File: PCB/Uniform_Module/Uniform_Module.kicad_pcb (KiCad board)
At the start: 2 copper layers, 301.5 x 93.4 mm, 186 parts, among them M1 MountingHole_2.7mm_M2.5, M10 MountingHole_2.7mm_M2.5, M2 MountingHole_2.7mm_M2.5, M3 MountingHole_2.7mm_M2.5, M4 MountingHole_2.7mm_M2.5, M5 MountingHole_2.7mm_M2.5, M6 MountingHole_2.7mm_M2.5, M7 MountingHole_2.7mm_M2.5, M8 MountingHole_2.7mm_M2.5, M9 MountingHole_2.7mm_M2.5, U1 STM32L072KZT6, U2 SN74AHCT1G125DBVR

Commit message: PCIE slot is upside down... began footprint, comitting changes and preparing to re-route on board :(
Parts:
- removed C1, C2: 10uf, ul_FG16X7R1E106KRT06:FG16X7R1E106KRT06
- removed C3, C4, C5: 0.1uf, Resistor_THT:R_Axial_DIN0207_L6.3mm_D2.5mm_P7.62mm_Horizontal
- removed C6: 1uf, RDER71H105K2M1H03A:CAP_RDER71H105K2M1H03A
- removed D_0_0, D_0_1, D_0_10, D_0_11, D_0_12, D_0_13, D_0_2, D_0_3, D_0_4, D_0_5, D_0_6, D_0_7, D_0_8, D_0_9, D_1_0, D_1_1, D_1_10, D_1_11, D_1_12, D_1_13, D_1_2, D_1_3, D_1_4, D_1_5, D_1_6, D_1_7, D_1_8, D_1_9, D_2_0, D_2_1, D_2_10, D_2_11, D_2_12, D_2_13, D_2_2, D_2_3, D_2_4, D_2_5, D_2_6, D_2_7, D_2_8, D_2_9, D_3_0, D_3_1, D_3_10, D_3_11, D_3_12, D_3_13, D_3_2, D_3_3, D_3_4, D_3_5, D_3_6, D_3_7, D_3_8, D_3_9, D_4_0, D_4_1, D_4_10, D_4_11, D_4_12, D_4_13, D_4_2, D_4_4, D_4_5, D_4_6, D_4_8, D_4_9: D, 1N4148:DIOAD829W49L456D191
- removed EM1, EM2, M1, M10, M2, M3, M4, M5, M6, M7, M8, M9: MountingHole_2.7mm_M2.5, MountingHole:MountingHole_2.7mm_M2.5
- removed G*** (x12): LOGO, Graphics:graphic_mounting_indicator
- removed G*** (x2): LOGO, Graphics:graphic_logo
- removed G***: LOGO, Graphics:graphic_designed-by-with-year
- removed K_0_0, K_0_1, K_0_10, K_0_11, K_0_12, K_0_13, K_0_2, K_0_3, K_0_4, K_0_5, K_0_6, K_0_7, K_0_8, K_0_9, K_1_0, K_1_1, K_1_10, K_1_11, K_1_12, K_1_13, K_1_2, K_1_3, K_1_4, K_1_5, K_1_6, K_1_7, K_1_8, K_1_9, K_2_0, K_2_1, K_2_10, K_2_11, K_2_12, K_2_13, K_2_2, K_2_3, K_2_4, K_2_5, K_2_6, K_2_7, K_2_8, K_2_9, K_3_0, K_3_1, K_3_10, K_3_11, K_3_12, K_3_13, K_3_2, K_3_3, K_3_4, K_3_5, K_3_6, K_3_7, K_3_8, K_3_9, K_4_0, K_4_1, K_4_10, K_4_11, K_4_12, K_4_13, K_4_2, K_4_4, K_4_5, K_4_6, K_4_8, K_4_9: KEYSW, keyswitches:SW_MX
- removed L1, L2, L3: NeoPixel_THT, Neopixel:LED_D5.0mm-4_RGB
- removed L4: Conn_01x03, Connector_PinHeader_2.54mm:PinHeader_1x03_P2.54mm_Vertical
- removed R1, R2: 5.1k, Resistor_THT:R_Axial_DIN0204_L3.6mm_D1.6mm_P7.62mm_Horizontal
- removed R3, R4: 10k, Resistor_THT:R_Axial_DIN0204_L3.6mm_D1.6mm_P7.62mm_Horizontal
- removed R5: R, Resistor_THT:R_Axial_DIN0309_L9.0mm_D3.2mm_P12.70mm_Horizontal
- removed R6: 330, Resistor_THT:R_Axial_DIN0309_L9.0mm_D3.2mm_P12.70mm_Horizontal
- removed S1, S2: OS102011MS2QN1, OS102011MS2QN1:SW_OS102011MS2QN1
- removed SWD1: 826629-5, 826629-5:TE_826629-5
- removed U1: STM32L072KZT6, STM32L072KZT6:QFP80P900X900X160-32N
- removed U2: SN74AHCT1G125DBVR, SN74AHCT1G125DBVR:SOT95P280X145-5N
- removed USBC1: USB4085-GF-A_REVA4, USB4085-GF-A_REVA4:GCT_USB4085-GF-A_REVA4
- removed VREG1: TLV1117-33, TLV1117-33IDCY:SOT230P700X180-4N
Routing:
- net C13: track 397.4 -> 0.00 mm, vias 2 -> 0
- net C12: track 366.4 -> 0.00 mm
- net C11: track 340.2 -> 0.00 mm
- net R0: track 327.5 -> 0.00 mm, vias 2 -> 0
- net C10: track 315.8 -> 0.00 mm
- net R1: track 306.9 -> 0.00 mm, vias 2 -> 0
- net R4: track 293.7 -> 0.00 mm
- net R2: track 291.3 -> 0.00 mm, vias 2 -> 0
- net C9: track 279.3 -> 0.00 mm
- net R3: track 275.6 -> 0.00 mm
- net C8: track 259.5 -> 0.00 mm
- net C6: track 222.0 -> 0.00 mm
- net C7: track 220.7 -> 0.00 mm
- net C5: track 200.3 -> 0.00 mm
- net GND: track 191.9 -> 0.00 mm, vias 1 -> 0
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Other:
- board outline removed
- board text removed: "BOOT->"
- board text removed: "RESET->"

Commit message: began routing for uniform module
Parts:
- added C1: 10uf, Capacitor_SMD:C_0603_1608Metric_Pad1.08x0.95mm_HandSolder, F.Cu at (199.3, 159.5)
- added C2: 10uf, Capacitor_SMD:C_0603_1608Metric_Pad1.08x0.95mm_HandSolder, F.Cu at (196.3, 149.5)
- added C3: 0.1uf, Capacitor_SMD:C_0603_1608Metric_Pad1.08x0.95mm_HandSolder, F.Cu at (229.3, 161.8)
- added C4: 0.1uf, Capacitor_SMD:C_0603_1608Metric_Pad1.08x0.95mm_HandSolder, F.Cu at (192.3, 149.5)
- added C5: 0.1uf, Capacitor_SMD:C_0603_1608Metric_Pad1.08x0.95mm_HandSolder, F.Cu at (193.5, 145.5)
- added C6: 1uf, Capacitor_SMD:C_0603_1608Metric_Pad1.08x0.95mm_HandSolder, F.Cu at (235.0, 168.2)
- added D1: LED, LED_SMD:LED_0603_1608Metric_Pad1.05x0.95mm_HandSolder, F.Cu at (230.0, 134.5)
- added J1: PCIE_x1_Conn_01x36_Male, Uniform:SAMTEC_PCIE_x1_CARD_EDGE_02_X_D_TH, F.Cu at (221.8, 156.0)
- added R1: 10k, Resistor_SMD:R_0603_1608Metric_Pad0.98x0.95mm_HandSolder, F.Cu at (239.3, 166.2)
- added R2: 10k, Resistor_SMD:R_0603_1608Metric_Pad0.98x0.95mm_HandSolder, F.Cu at (235.0, 170.7)
- added R3: 100, Resistor_SMD:R_0603_1608Metric_Pad0.98x0.95mm_HandSolder, F.Cu at (198.8, 155.5)
- added SW1: Button_SMD_PTS_647_SN50_SMTR2_LFS, Uniform:Button SMD PTS 647 SN50 SMTR2 LFS, F.Cu at (246.0, 133.7)
- added SW2: Button_SMD_PTS_647_SN50_SMTR2_LFS, Uniform:Button SMD PTS 647 SN50 SMTR2 LFS, F.Cu at (248.8, 140.7)
- added SWD1: PH1RB-05-UA, Connector_PinHeader_2.54mm:PinHeader_1x05_P2.54mm_Vertical, F.Cu at (209.5, 138.7)
- added U1: STM32L072KZT6, STM32L072KZT6:QFP80P900X900X160-32N, F.Cu at (222.3, 142.0)
- added VREG1: TLV1117-33, TLV1117-33IDCY:SOT230P700X180-4N, F.Cu at (207.5, 145.5)
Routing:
- net PA7: track 0.00 -> 33.0 mm, vias 0 -> 1
- net PA6: track 0.00 -> 33.0 mm, vias 0 -> 1
- net PA5: track 0.00 -> 33.0 mm, vias 0 -> 1
- net PA4: track 0.00 -> 33.0 mm, vias 0 -> 1
- net PA3: track 0.00 -> 32.9 mm, vias 0 -> 1
- net PB4: track 0.00 -> 27.6 mm, vias 0 -> 2
- net PB5: track 0.00 -> 25.5 mm, vias 0 -> 2
- net PB6: track 0.00 -> 22.4 mm, vias 0 -> 2
- net PB7: track 0.00 -> 20.6 mm
- net PC14: track 0.00 -> 13.1 mm, vias 0 -> 1
- net PC15: track 0.00 -> 12.7 mm, vias 0 -> 1
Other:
- board outline added: 20.3 x 8.4 mm

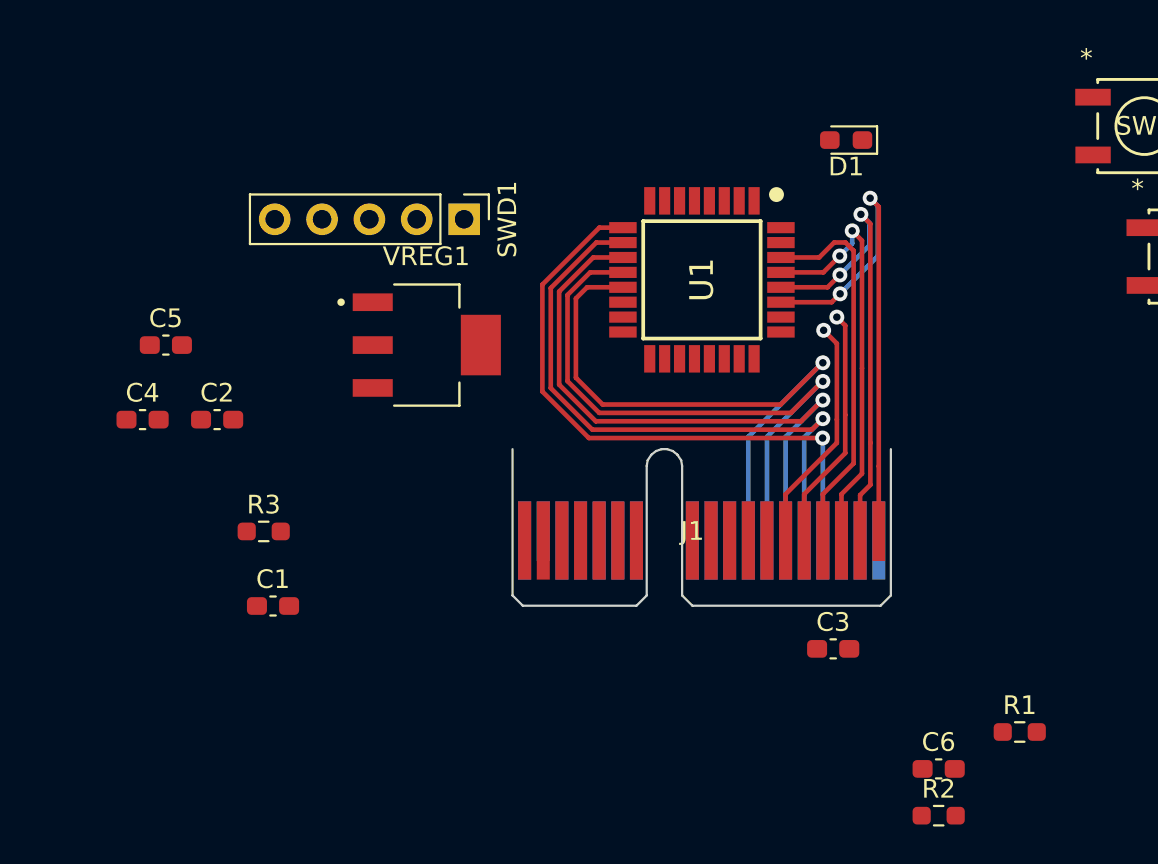
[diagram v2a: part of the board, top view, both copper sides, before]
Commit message: clear all routing on module. Fix incorrect PCIE edge connector schematic net assignments
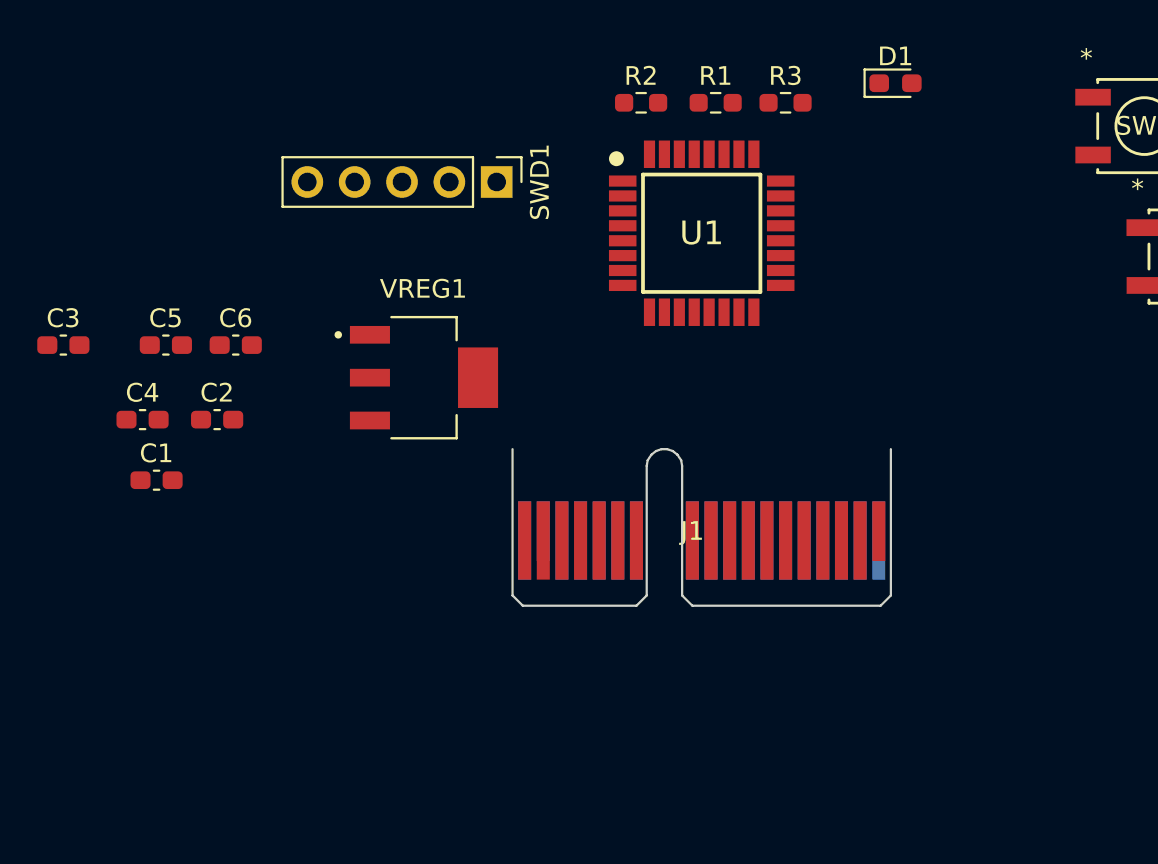
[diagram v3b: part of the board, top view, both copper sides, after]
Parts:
- moved C3 44.4 mm to (188.0, 145.5)
- moved C6 44.0 mm to (197.3, 145.5)
- moved R2 41.4 mm to (219.0, 132.5)
- moved R1 37.5 mm to (223.0, 132.5)
- moved R3 36.2 mm to (226.8, 132.5)
- moved C1 9.20 mm to (193.0, 152.7)
- moved D1 4.04 mm to (232.7, 131.4), turned to 0 degrees
- moved SWD1 2.66 mm to (211.3, 136.7)
- moved U1 2.50 mm to (222.3, 139.5), turned to 0 degrees
- moved VREG1 1.76 mm to (207.4, 147.2)
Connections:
- J1 pad 1: PB4 -> +5V
- J1 pad 10: unconnected-(J1-Pad10) -> PA5
- J1 pad 11: unconnected-(J1-Pad11) -> PA4
- J1 pad 12: unconnected-(J1-Pad12) -> PA3
- J1 pad 13: unconnected-(J1-Pad13) -> PA2
- J1 pad 14: D_P -> PA1
- J1 pad 15: unconnected-(J1-Pad15) -> PA0
- J1 pad 16: D_N -> unconnected-(J1-Pad16)
- J1 pad 17: GND -> unconnected-(J1-Pad17)
- J1 pad 18: +5V -> unconnected-(J1-Pad18)
- J1 pad 19: PA0 -> GND
- J1 pad 2: PB5 -> PA15
- J1 pad 20: PA1 -> D_P
- J1 pad 21: PA2 -> D_N
- J1 pad 22: PA3 -> PB3
- J1 pad 23: PA4 -> PB4
- J1 pad 24: PA5 -> PB5
- J1 pad 25: PA6 -> PB6
- J1 pad 26: PA7 -> PB7
- J1 pad 27: PA8 -> PC14
- J1 pad 28: PA9 -> PC15
- J1 pad 29: PA10 -> unconnected-(J1-Pad29)
- J1 pad 3: PB6 -> PA10
- J1 pad 30: PA11 -> unconnected-(J1-Pad30)
- J1 pad 31: PA12 -> unconnected-(J1-Pad31)
- J1 pad 32: PB0 -> unconnected-(J1-Pad32)
- J1 pad 33: PB1 -> unconnected-(J1-Pad33)
- J1 pad 34: PB3 -> unconnected-(J1-Pad34)
- J1 pad 35: GND -> unconnected-(J1-Pad35)
- J1 pad 4: PB7 -> PA9
- J1 pad 5: PC14 -> PA8
- J1 pad 6: PC15 -> PB1
- J1 pad 7: unconnected-(J1-Pad7) -> PB0
- J1 pad 8: unconnected-(J1-Pad8) -> PA7
- J1 pad 9: unconnected-(J1-Pad9) -> PA6
- U1 pad 21: PA11 -> D_N
- U1 pad 22: PA12 -> D_P
- U1 pad 25: STATUS_LED -> PA15
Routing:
- net PA7: track 33.0 -> 0.00 mm, vias 1 -> 0
- net PA6: track 33.0 -> 0.00 mm, vias 1 -> 0
- net PA5: track 33.0 -> 0.00 mm, vias 1 -> 0
- net PA4: track 33.0 -> 0.00 mm, vias 1 -> 0
- net PA3: track 32.9 -> 0.00 mm, vias 1 -> 0
- net PB4: track 27.6 -> 0.00 mm, vias 2 -> 0
- net PB5: track 25.5 -> 0.00 mm, vias 2 -> 0
- net PB6: track 22.4 -> 0.00 mm, vias 2 -> 0
- net PB7: track 20.6 -> 0.00 mm
- net PC14: track 13.1 -> 0.00 mm, vias 1 -> 0
- net PC15: track 12.7 -> 0.00 mm, vias 1 -> 0

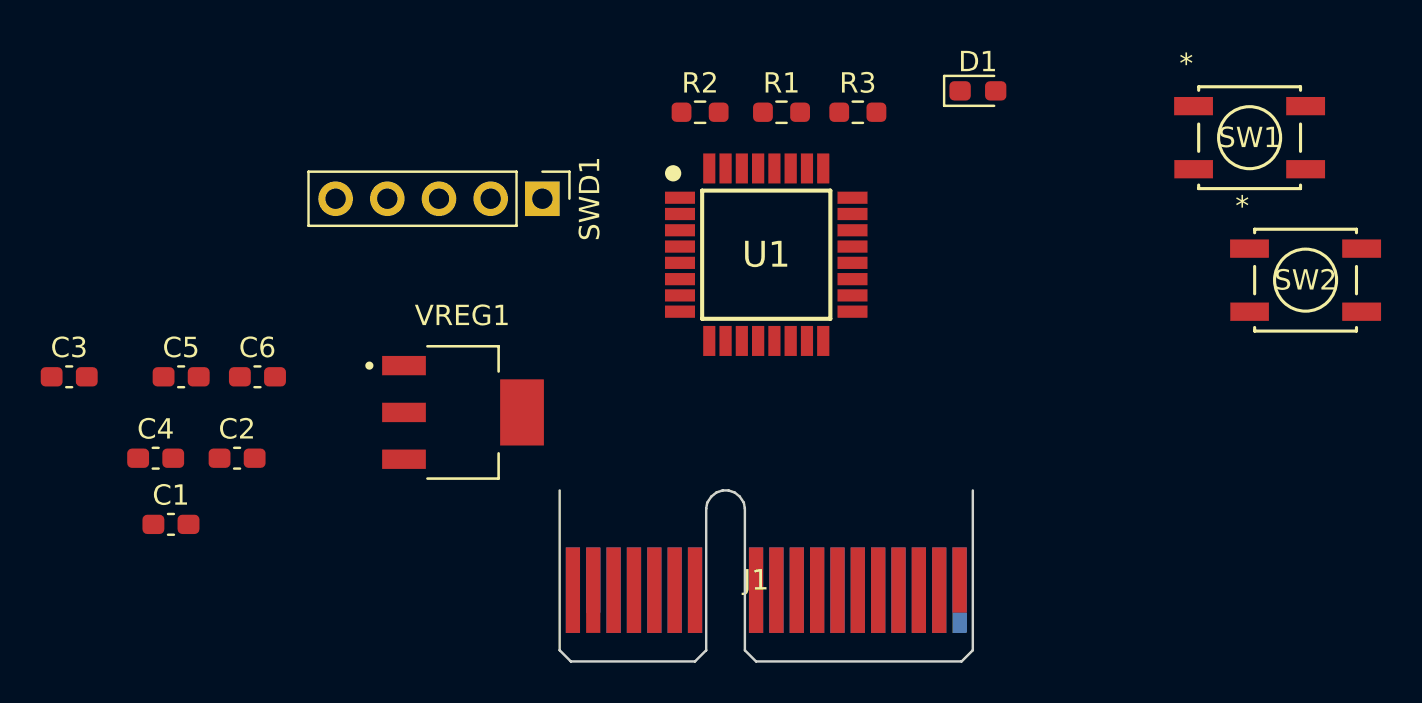
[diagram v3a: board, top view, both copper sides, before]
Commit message: improved trace origins on PCIE port/edge. Board rerouting done. Module rerouting in progress
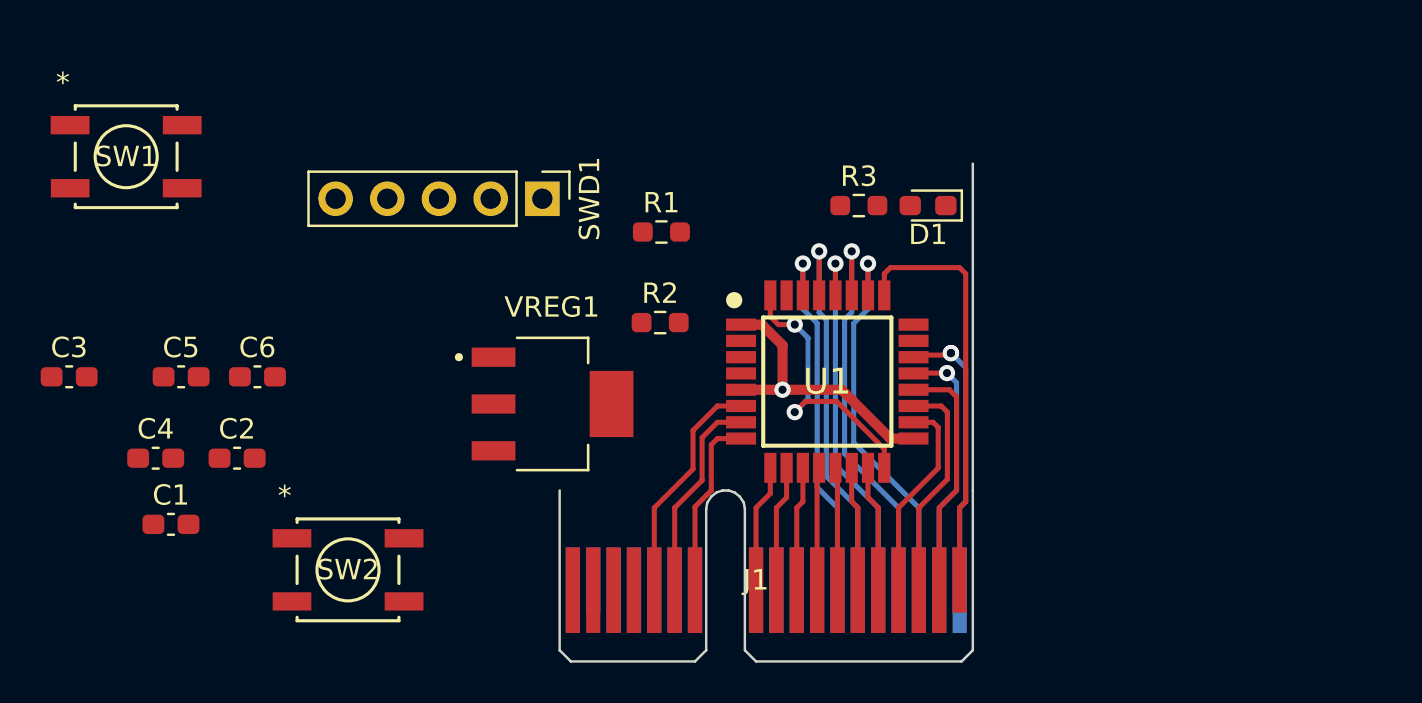
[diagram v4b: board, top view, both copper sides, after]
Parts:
- moved SW1 55.2 mm to (190.8, 134.7)
- moved SW2 49.2 mm to (201.7, 155.0)
- moved R2 10.5 mm to (217.1, 142.8)
- moved R1 8.33 mm to (217.1, 138.4)
- moved U1 6.92 mm to (225.3, 145.7)
- moved D1 6.14 mm to (230.2, 137.1), turned to 180 degrees
- moved R3 4.59 mm to (226.8, 137.1)
- moved VREG1 4.42 mm to (211.8, 146.8)
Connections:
- J1 pad 1: +5V -> PA15
- J1 pad 10: PA5 -> PA4
- J1 pad 11: PA4 -> PA3
- J1 pad 12: PA3 -> PA2
- J1 pad 13: PA2 -> PA1
- J1 pad 14: PA1 -> PA0
- J1 pad 15: PA0 -> unconnected-(J1-Pad15)
- J1 pad 18: unconnected-(J1-Pad18) -> +5V
- J1 pad 19: GND -> D_P
- J1 pad 2: PA15 -> PA10
- J1 pad 20: D_P -> D_N
- J1 pad 21: D_N -> PB3
- J1 pad 22: PB3 -> PB4
- J1 pad 23: PB4 -> PB5
- J1 pad 24: PB5 -> PB6
- J1 pad 25: PB6 -> PB7
- J1 pad 26: PB7 -> PC14
- J1 pad 27: PC14 -> PC15
- J1 pad 28: PC15 -> unconnected-(J1-Pad28)
- J1 pad 3: PA10 -> PA9
- J1 pad 36: unconnected-(J1-Pad36) -> GND
- J1 pad 4: PA9 -> PA8
- J1 pad 5: PA8 -> PB1
- J1 pad 6: PB1 -> PB0
- J1 pad 7: PB0 -> PA7
- J1 pad 8: PA7 -> PA6
- J1 pad 9: PA6 -> PA5
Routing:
- net PA15: track 0.00 -> 20.5 mm
- net PB4: track 0.00 -> 20.1 mm, vias 0 -> 1
- net PB6: track 0.00 -> 19.6 mm, vias 0 -> 1
- net PB3: track 0.00 -> 19.2 mm, vias 0 -> 1
- net PB5: track 0.00 -> 18.5 mm, vias 0 -> 1
- net PB7: track 0.00 -> 18.3 mm, vias 0 -> 1
- net +3V3: track 0.00 -> 14.1 mm, vias 0 -> 1
- net D_P: track 0.00 -> 14.0 mm, vias 0 -> 2
- net GND: track 0.00 -> 13.8 mm, vias 0 -> 2
- net D_N: track 0.00 -> 12.9 mm, vias 0 -> 1
- net PA10: track 0.00 -> 12.1 mm
- net PA0: track 0.00 -> 11.5 mm
- net PA9: track 0.00 -> 11.1 mm
- net PA1: track 0.00 -> 10.3 mm
- net PA8: track 0.00 -> 10.1 mm
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
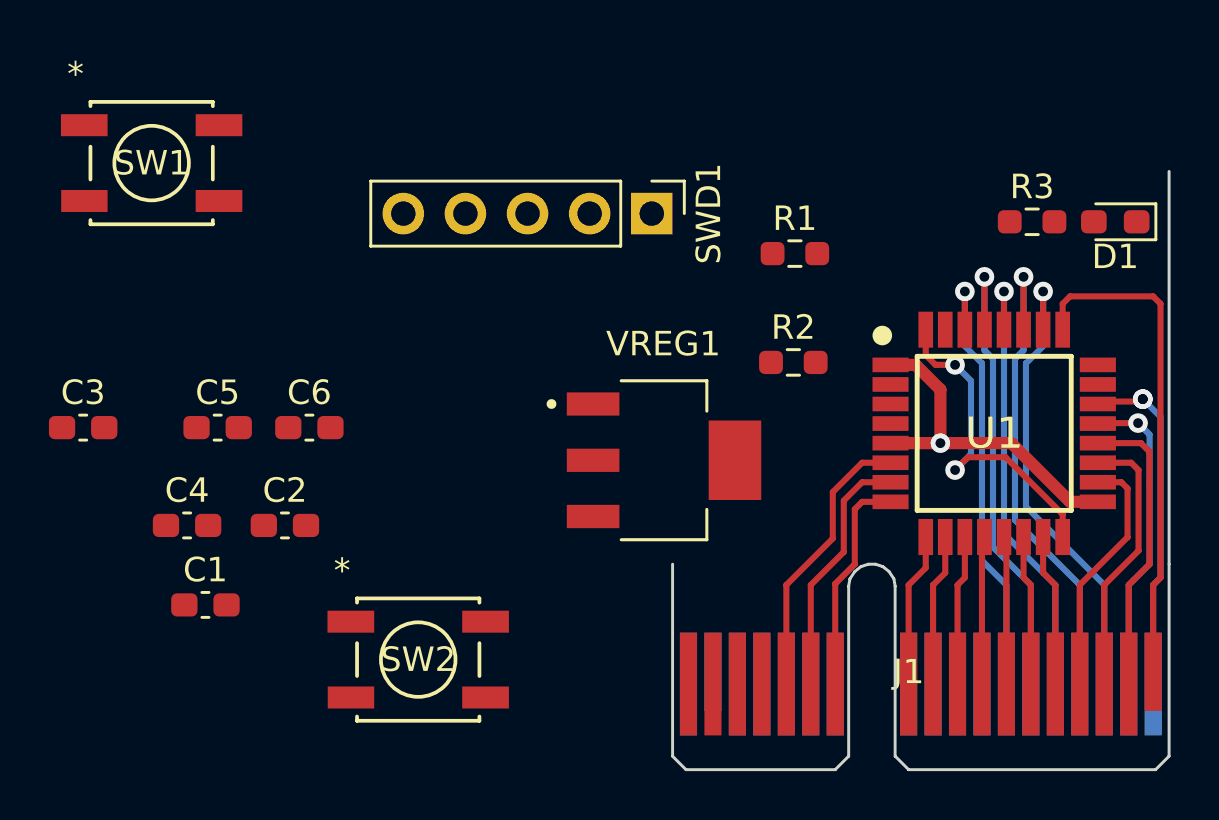
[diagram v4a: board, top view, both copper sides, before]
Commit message: first pass at module layout. silkscreen added
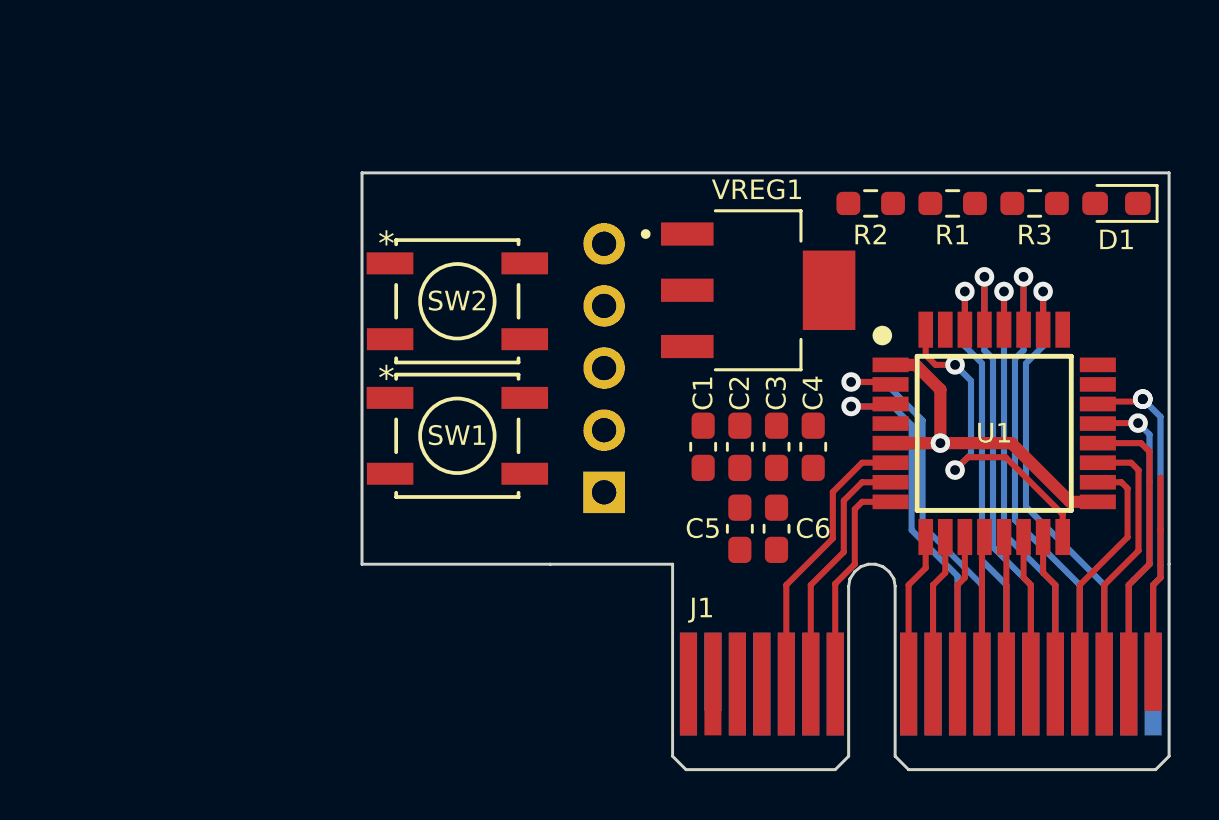
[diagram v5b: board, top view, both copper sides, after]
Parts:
- added G***: LOGO, Uniform:graphic_logo, B.Cu at (225.9, 136.8)
- SWD1: moved to B.Cu
- moved C3 28.4 mm to (216.4, 146.3), turned to -90 degrees
- moved C4 25.8 mm to (217.9, 146.3), turned to -90 degrees
- moved C5 21.7 mm to (214.9, 149.6), turned to 90 degrees
- moved C1 21.4 mm to (213.4, 146.3), turned to 90 degrees
- moved C6 19.5 mm to (216.4, 149.6), turned to 90 degrees
- moved C2 18.9 mm to (214.9, 146.3), turned to -90 degrees
- moved SW1 16.8 mm to (203.3, 145.8)
- moved SW2 14.7 mm to (203.3, 140.3)
- moved SWD1 11.6 mm to (209.3, 148.1), turned to 0 degrees
- moved VREG1 7.95 mm to (215.6, 139.9)
- moved R2 7.23 mm to (220.2, 136.3)
- moved R1 6.77 mm to (223.6, 136.3), turned to 180 degrees
- moved R3 0.76 mm to (226.9, 136.3)
- moved D1 0.75 mm to (230.3, 136.3)
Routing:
- net PC14: track 0.00 -> 17.0 mm, vias 0 -> 1
- net PC15: track 0.00 -> 15.8 mm, vias 0 -> 1
- net PA15: track 20.5 -> 8.07 mm
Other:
- board size 20.3 x 8.4 mm -> 33 x 16 mm
- board text added: "V2.00"
